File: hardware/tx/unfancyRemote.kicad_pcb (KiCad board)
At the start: 2 copper layers, 23.9 x 37 mm, 57 parts, among them J1 Battery, J3 HALL1/PPM, J4 HALL2, J6 VIN, J8 Motor, Q1 AO3401A, Q2 MMBT3904, Q3 MMBT3904, SW1 SW_Push, U1 E28-2G4M12S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

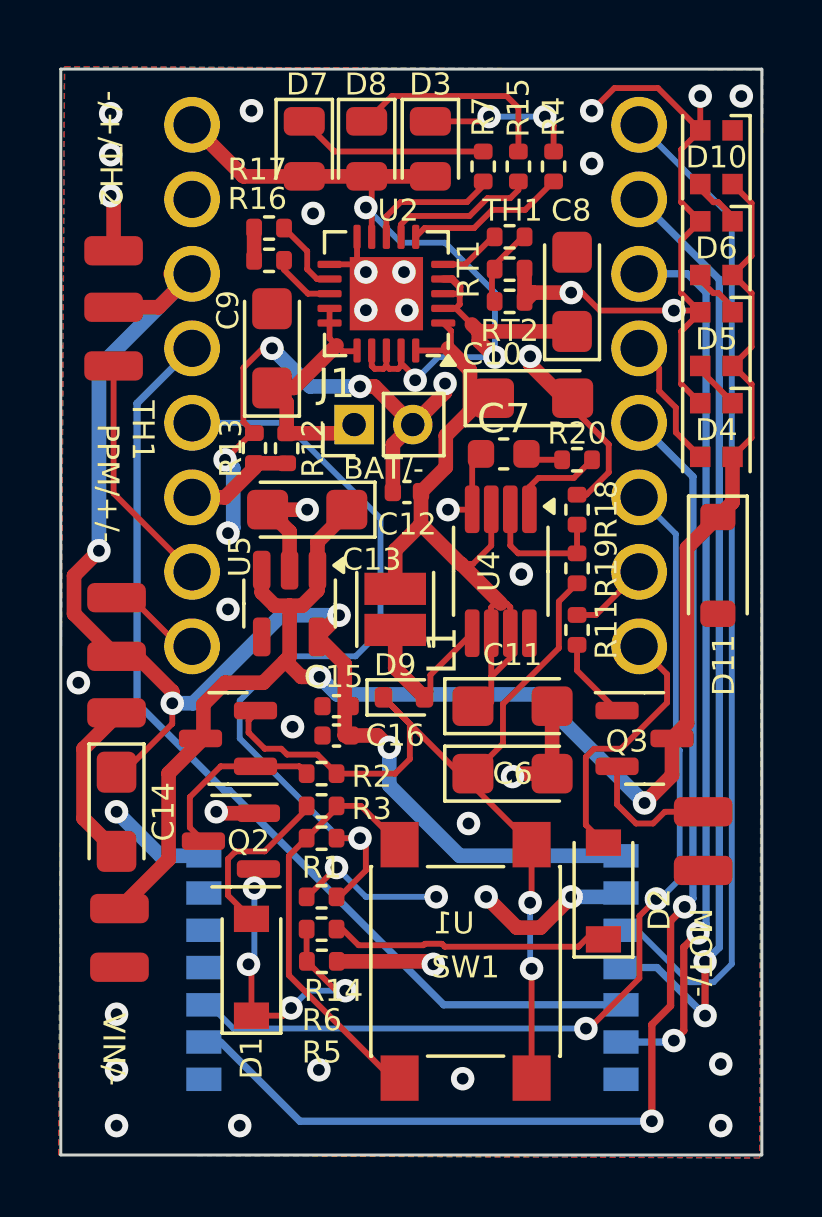
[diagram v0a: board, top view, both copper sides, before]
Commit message: update to kicad 9
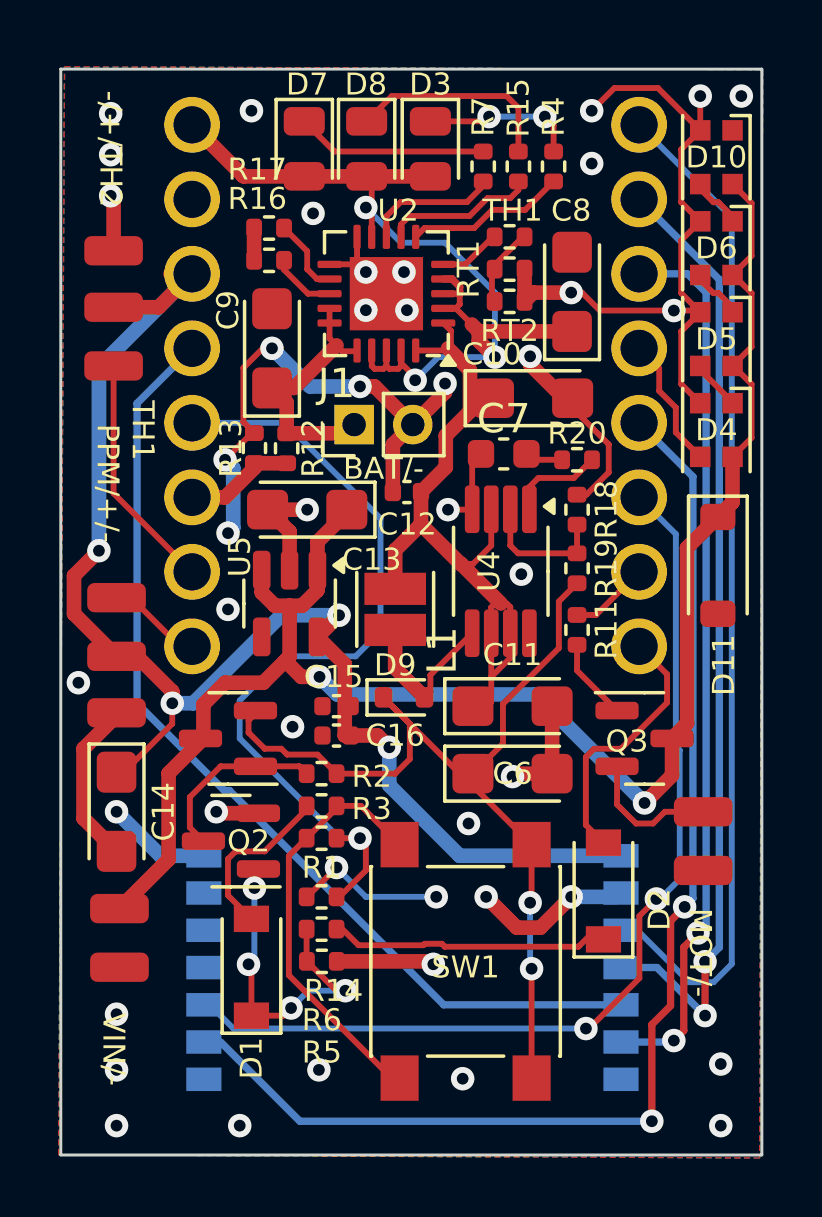
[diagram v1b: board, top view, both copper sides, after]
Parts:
- R13: value 6.8K -> 100K

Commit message: optimize all the things
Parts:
- moved D4 3.33 mm to (143.3, 79.4)
- moved D11 2.80 mm to (143.5, 83.5)
- moved D5 2.06 mm to (143.3, 75.0)
- moved D7 1.00 mm to (128.3, 66.5)
- moved R4 1.00 mm to (138.8, 67.1)
- moved R15 0.90 mm to (137.5, 67.1)
- moved R7 0.80 mm to (136.2, 67.1)
- moved D6 0.79 mm to (143.3, 70.7)
- moved D3 0.60 mm to (134.2, 66.5)
- moved D10 0.48 mm to (143.3, 66.3)
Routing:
- net GND: track 88.6 -> 84.6 mm, vias 44 -> 45
- net LED: track 4.56 -> 7.90 mm
- net Net-(D7-K): track 6.53 -> 8.37 mm
- net +3V3: track 48.9 -> 47.2 mm
- net Net-(D10-DIN): track 1.49 -> 3.00 mm
- net Net-(D5-DOUT): track 1.49 -> 2.96 mm
- net Net-(D4-DOUT): track 1.56 -> 2.86 mm
- net /MOSI: track 32.7 -> 33.8 mm
- net /RFBUSY: track 33.3 -> 34.4 mm
- net Net-(U2-STAT1/~{LBO}): track 4.43 -> 5.29 mm
- net Net-(U2-~{PG}): track 5.48 -> 6.34 mm
- net /MISO: track 34.7 -> 35.5 mm
- net Net-(D8-K): track 7.19 -> 7.91 mm
- net VBAT: track 9.34 -> 8.68 mm
- net Net-(U2-STAT2): track 5.21 -> 5.81 mm
